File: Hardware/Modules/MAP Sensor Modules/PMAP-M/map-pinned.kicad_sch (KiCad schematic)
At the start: 3 parts, among them IC1 Map, IC2 Baro, J1 Conn_02x03_Odd_Even

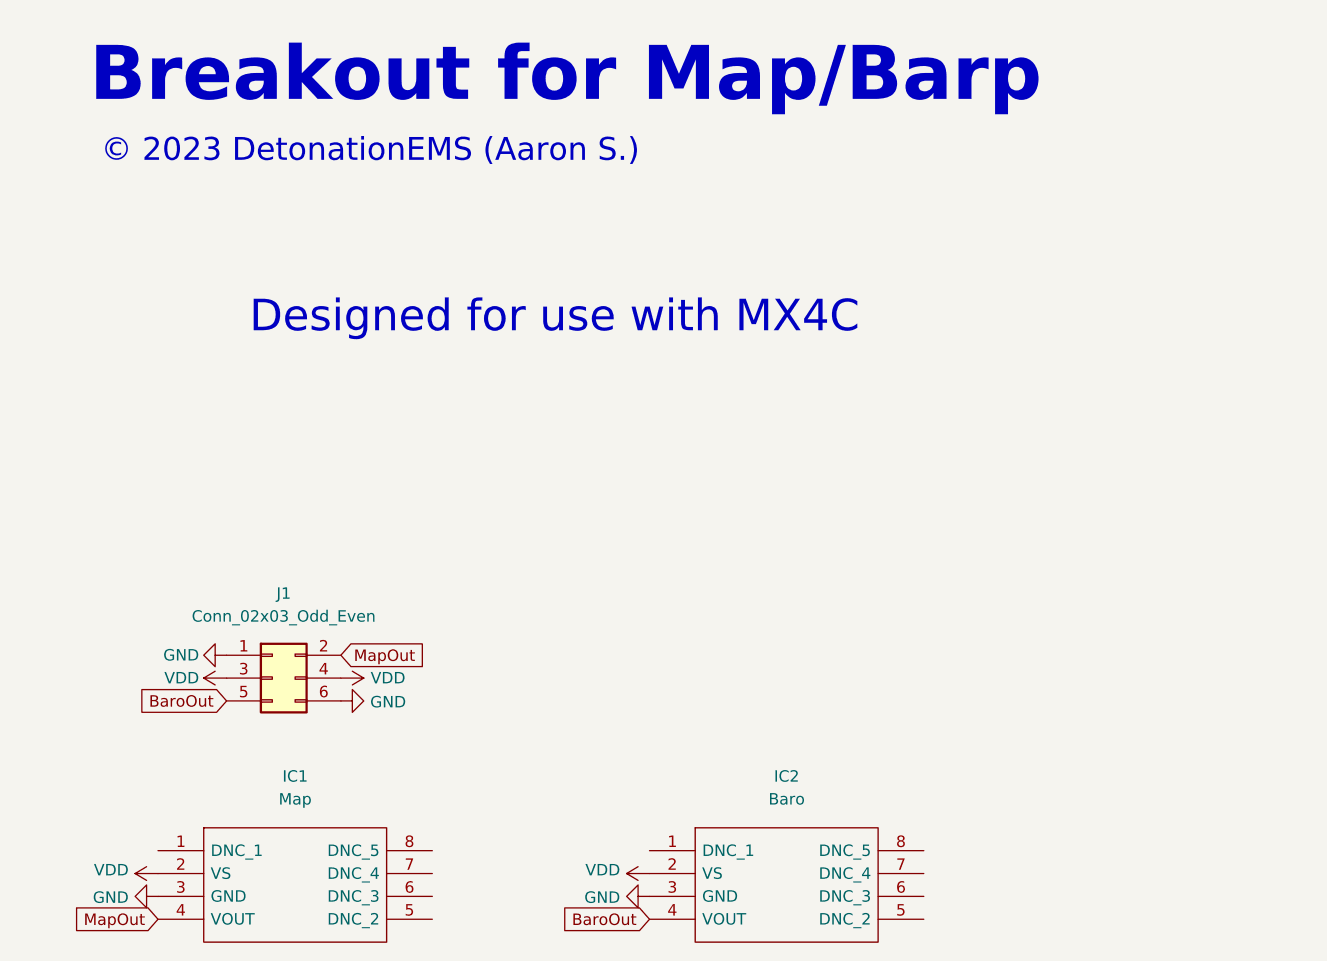
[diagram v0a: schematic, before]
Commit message: Initial upload PMAP-M
Updated map sensor design for OpenLogicEFI ECU's.

SHOULD NOT BE USED FOR BOARDS LABLED "DETONATIONEMS".
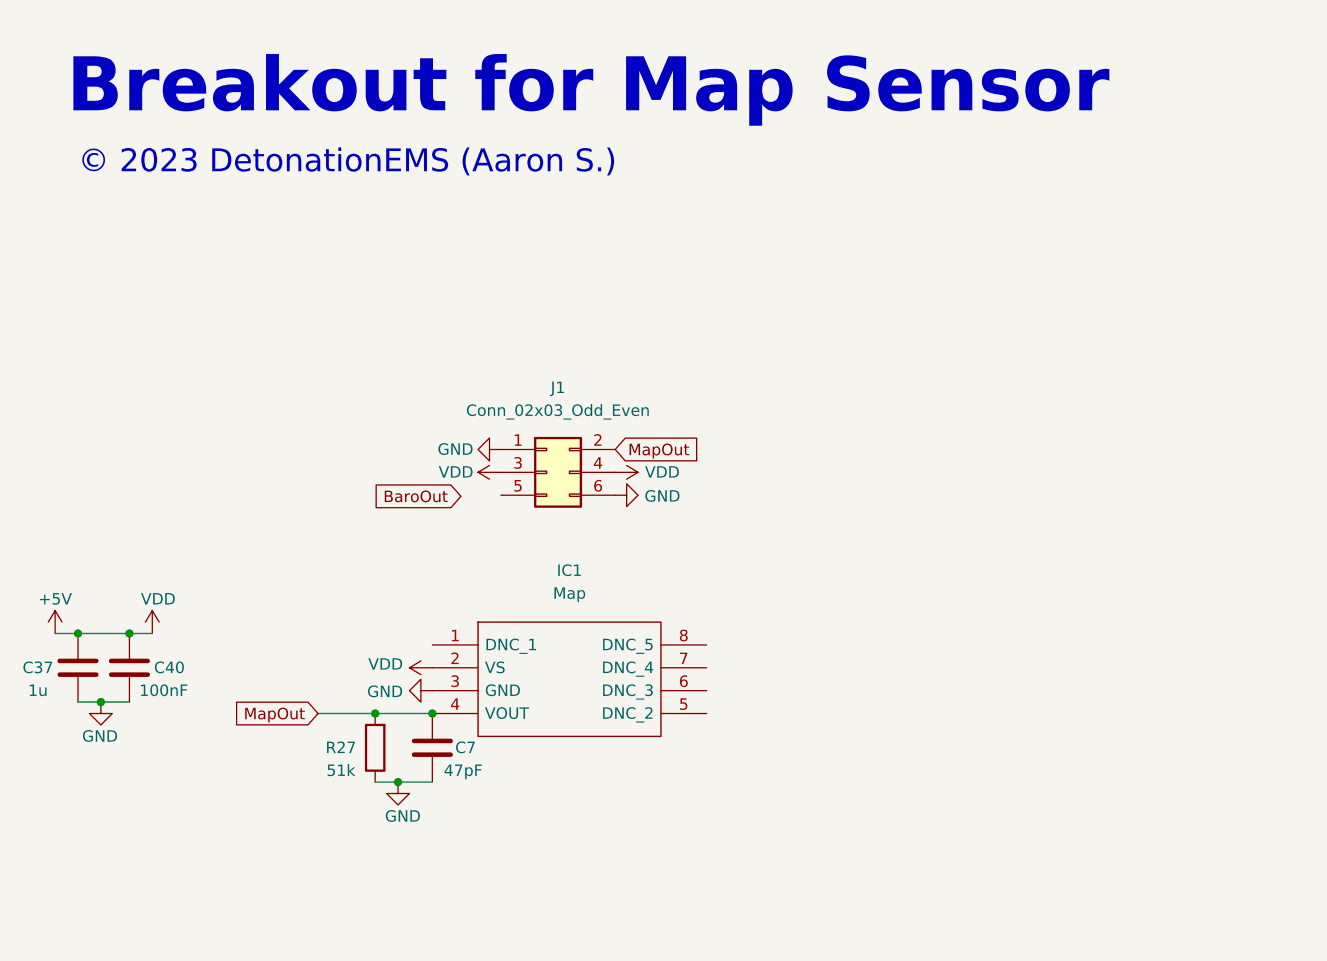
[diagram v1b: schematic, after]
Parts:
- removed IC2: Baro, Detonation:MPXH6250, symbol MPXH6250AC6U:MPXH6250AC6U
- added C37: 1u, Capacitor_SMD:C_0402_1005Metric, symbol Device:C
- added C40: 100nF, Capacitor_SMD:C_0402_1005Metric, symbol Device:C
- added C7: 47pF, Capacitor_SMD:C_0402_1005Metric, symbol Device:C
- added R27: 51k, Resistor_SMD:R_0402_1005Metric, symbol Device:R
- IC1: footprint Detonation:MPXH6250 -> Detonation:MPXHxxx_Handsoldering; now left out of the parts list
- J1: now left out of the parts list
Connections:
- net BaroOut: no longer J1.5 (Pin_5)
- net GND: now also C37.2, C40.2, C7.2, R27.1
- net MapOut: now also C7.1, R27.2
- net VDD renamed +5V
- net +5V: now also C37.1, C40.1
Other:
- note added: "Breakout for Map Sensor"
- note removed: "Breakout for Map/Barp"
- note removed: "Designed for use with MX4C"
- moved on the sheet: IC1, J1

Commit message: Minor updates
PMAP-M correction
Endcap updates
readme updates
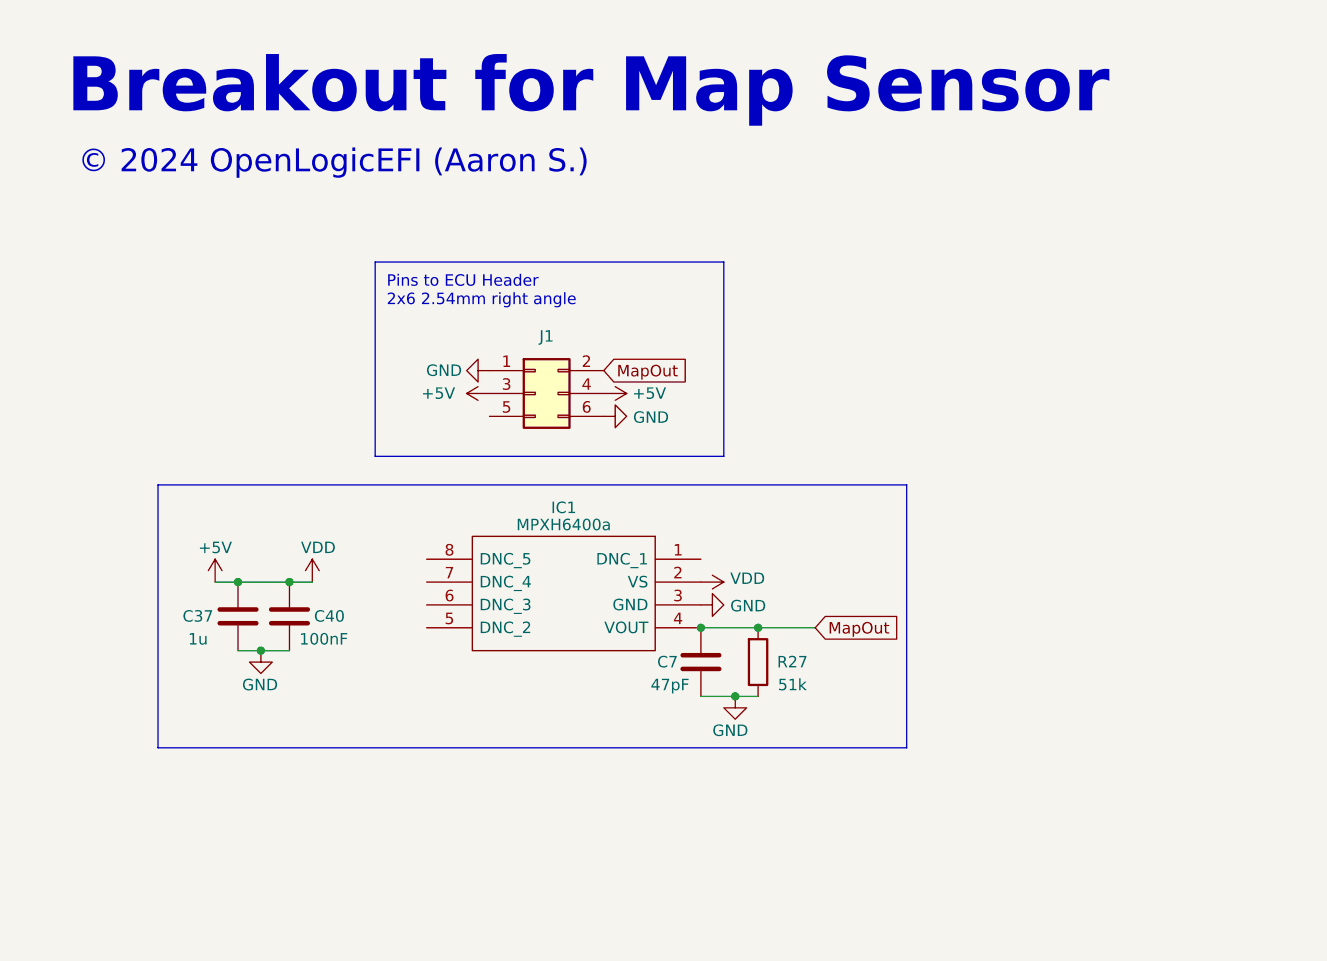
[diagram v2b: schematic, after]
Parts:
- IC1: value Map -> MPXH6400a
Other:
- note added: "Pins to ECU Header 2x6 2.54mm right angle"
- note added: "© 2024 OpenLogicEFI (Aaron S.)"
- note removed: "© 2023 DetonationEMS (Aaron S.)"
- company: (none) -> OpenLogicEFI
- title: (none) -> PMAP-M
- moved on the sheet: C37, C40, C7, IC1, J1, R27

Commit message: minor document changes
CD pinout zip
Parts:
- C2: renamed from C40; LCSC C307331 -> C1525; Manufacture Part Number (none) -> CL05B104KO5NNNC
- C3: renamed from C37; footprint Capacitor_SMD:C_0402_1005Metric -> Capacitor_SMD:C_0805_2012Metric; LCSC C52923 -> C28323; Manufacture Part Number (none) -> CL21B105KBFNNNE
- renumbered C7 to C1, R27 to R1
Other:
- note added: "© 2025 OpenLogicEFI (Aaron S.)"
- note removed: "© 2024 OpenLogicEFI (Aaron S.)"
